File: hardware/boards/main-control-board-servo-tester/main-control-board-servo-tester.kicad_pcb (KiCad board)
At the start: 2 copper layers, 30 x 11 mm, 5 parts, among them J1 Conn_01x03_Socket

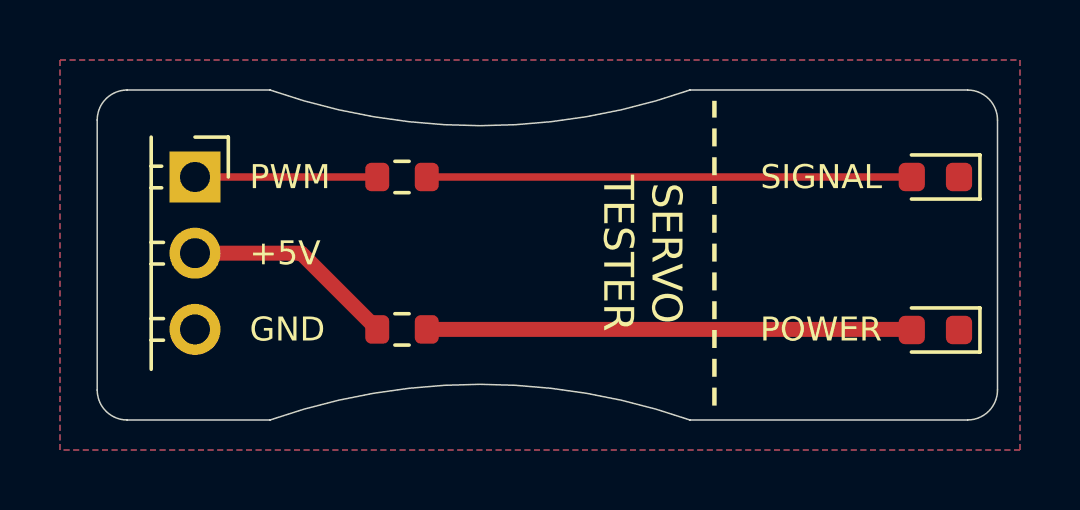
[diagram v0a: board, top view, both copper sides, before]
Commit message: fix(pcb): update net names and adjust component placements for improved layout
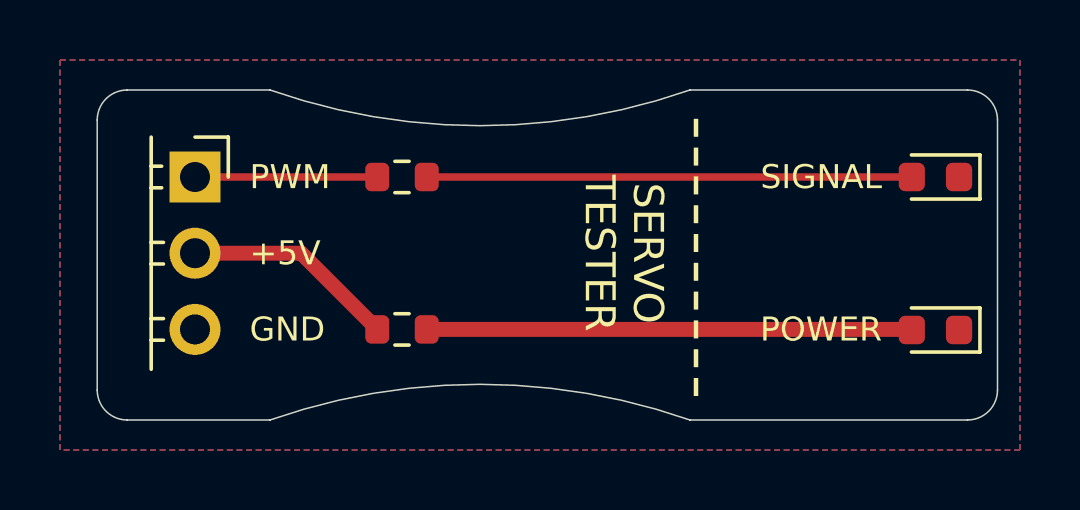
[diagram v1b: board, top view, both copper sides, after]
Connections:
- net Net-(D1-A) renamed /YELLOW_PWR
- net Net-(D2-A) renamed /RED_PWR
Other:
- board text added: "R1 · MAIN R3 2026-10-31"
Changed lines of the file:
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@@
 			(layers "F.Cu" "F.Mask" "F.Paste")
 			(roundrect_rratio 0.25)
-			(net "Net-(D1-A)")
+			(net "/YELLOW_PWR")
 			(pintype "passive")
 		)
@@
 			(layers "F.Cu" "F.Mask" "F.Paste")
 			(roundrect_rratio 0.25)
-			(net "Net-(D2-A)")
+			(net "/RED_PWR")
 			(pintype "passive")
 		)
@@
 			(layers "F.Cu" "F.Mask" "F.Paste")
 			(roundrect_rratio 0.25)
-			(net "Net-(D1-A)")
+			(net "/YELLOW_PWR")
 			(pinfunction "A_2")
 			(pintype "passive")
@@
 			(layers "F.Cu" "F.Mask" "F.Paste")
 			(roundrect_rratio 0.25)
-			(net "Net-(D2-A)")
+			(net "/RED_PWR")
 			(pinfunction "A_2")
 			(pintype "passive")
@@
 	)
 	(gr_line
-		(start 162.814 96.52)
-		(end 162.814 86.36)
+		(start 162.2 96.2)
+		(end 162.2 86.6)
 		(stroke
 			(width 0.15)
@@
 	)
 	(gr_line
+		(start 162.2 96.3)
+		(end 162.2 86.7)
+		(stroke
+			(width 0.15)
+			(type dot)
+		)
+		(layer "B.SilkS")
+	)
+	(gr_line
 		(start 142.24 87)
 		(end 142.24 96)
@@
 	)
 	(gr_text "SERVO\nTESTER"
-		(at 161.798 91.44 270)
+		(at 161.184 91.44 270)
 		(layer "F.SilkS")
 		(effects
@@
 			)
 			(justify top)
+		)
+	)
+	(gr_text "R1 · MAIN R3\n2026-10-31"
+		(at 167.2 91.7 0)
+		(layer "B.SilkS")
+		(effects
+			(font
+				(size 0.7 0.7)
+				(thickness 0.1)
+			)
+			(justify top mirror)
 		)
 	)
@@
 		)
 	)
+	(gr_text "SERVO TESTER"
+		(at 167.1 89.7 0)
+		(layer "B.SilkS")
+		(effects
+			(font
+				(size 0.8 0.8)
+				(thickness 0.14)
+				(bold yes)
+			)
+			(justify top mirror)
+		)
+	)
 	(segment
 		(start 145.5 88.9)
@@
 		(width 0.25)
 		(layer "F.Cu")
-		(net "Net-(D1-A)")
+		(net "/YELLOW_PWR")
 	)
 	(segment
@@
 		(width 0.5)
 		(layer "F.Cu")
-		(net "Net-(D2-A)")
+		(net "/RED_PWR")
 	)
 	(segment
@@
 		(width 0.5)
 		(layer "F.Cu")
-		(net "Net-(D2-A)")
+		(net "/RED_PWR")
 	)
 	(zone
